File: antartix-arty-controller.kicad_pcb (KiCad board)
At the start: 4 copper layers, 96 x 40 mm, 163 parts, among them IC1 FT2232D, IC2 TPD8S009DSMR, J1 QTE-020-04-L-D-A, J10 3-794680-8, J11 1-794610-1, J12 1-794610-1, J13 1-794610-1, J14 1-794610-1, J15 3-794617-8, J16 1-794610-1, J17 1-794610-1, J18 1-794610-1, J19 1-794610-1, J2 0022232041, J3 614004185023, J4 WE_629105150521, J5 614004185023, J6 614004185023, J7 QTE-020-04-L-D-A, J8 WE_629105150521, J9 WE_685119136923, Q1 FDC6330L, Q2 FDC6330L, Q3 FDC6330L, U1 PCT2075GVX, U2 PAC1934T-I_JQ, U3 USB2514B-I_M2, U4 TPS2024DR, U5 TPS2024DR, U6 TPS2024DR, U7 FT230XS-R, Y1 7C-24.000MBB-T, Y2 MQ-6.000-12-30_30_

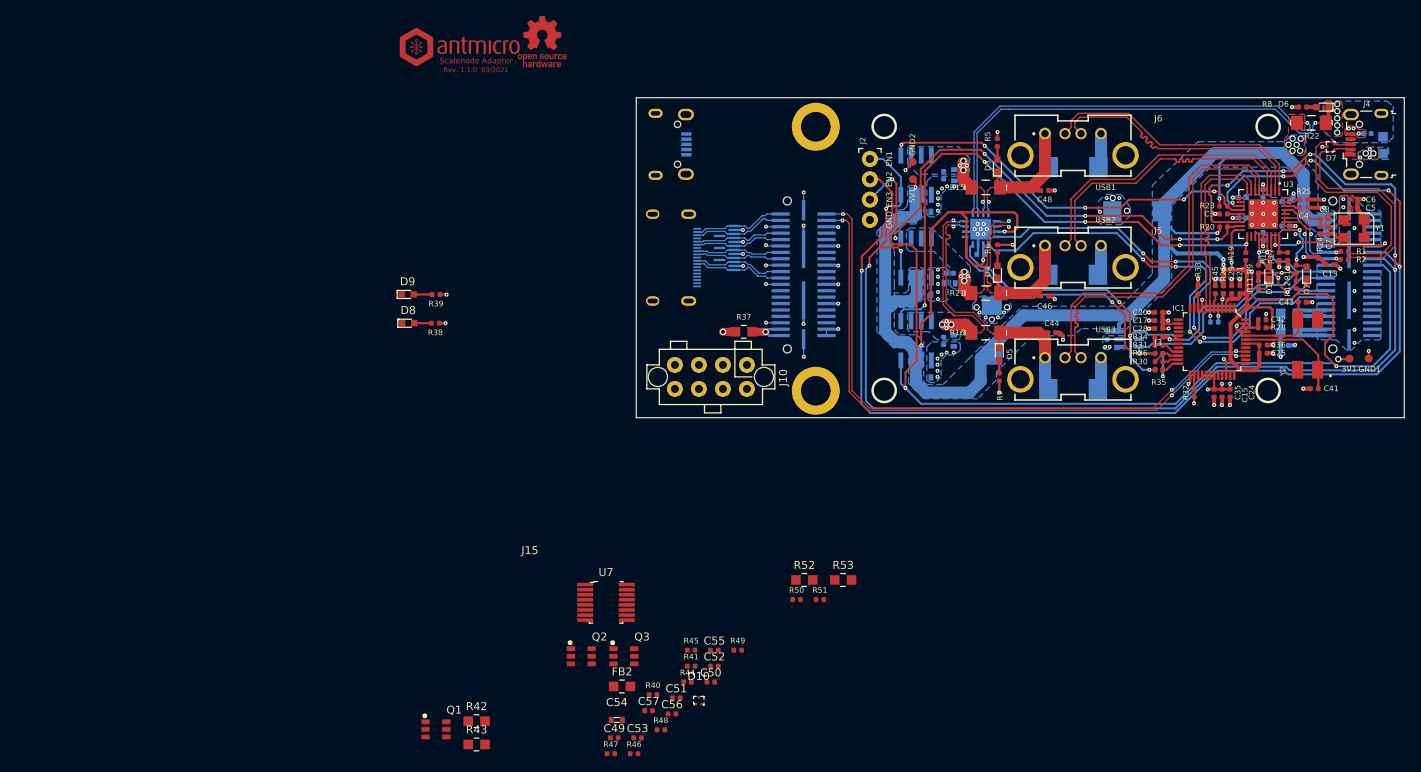
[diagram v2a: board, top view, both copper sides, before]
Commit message: Route buttons and HDMI
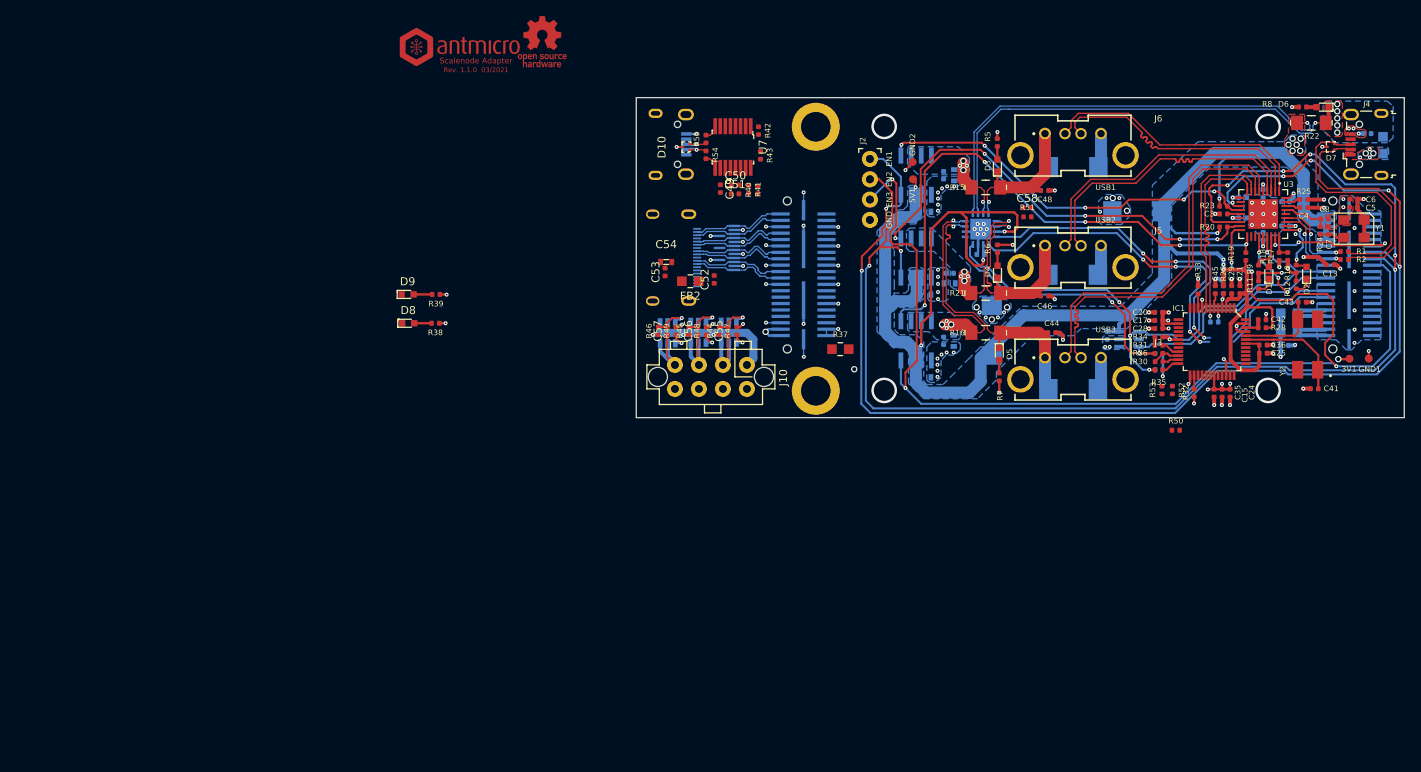
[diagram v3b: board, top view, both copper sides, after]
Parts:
- added C58: C_100n_0402, antartix-arty-controller-footprints:0402-cap, F.Cu at (190.9, 86.3)
- added R54: R_22R_0402, antartix-arty-controller-footprints:0402-res, F.Cu at (150.7, 79.7)
- added R55: R_22R_0402, antartix-arty-controller-footprints:0402-res, F.Cu at (150.7, 77.7)
- J11, J12, J13, J14, J15, J16, J17, J18, J19, Q1, Q2, Q3: moved to B.Cu
- R42, R43, R52, R53: value R_0R_0805 -> R_0R_0402; footprint antmicro-footprints:0805-res -> antartix-arty-controller-footprints:0402-res
- moved R42 81.8 mm to (157.3, 76.6), turned to 270 degrees
- moved R43 81.7 mm to (157.5, 79.7), turned to 270 degrees
- moved C49 69.9 mm to (152.5, 83.9), turned to 270 degrees
- moved D10 69.2 mm to (148.3, 78.7), turned to 90 degrees
- moved R40 64.5 mm to (157.2, 84.0), turned to 90 degrees
- moved C51 63.4 mm to (154.3, 84.5)
- moved C50 62.2 mm to (154.4, 83.4)
- moved Q1 61.7 mm to (153.6, 101.8), turned to 90 degrees
- moved R41 60.0 mm to (156.0, 84.0), turned to 270 degrees
- moved U7 59.1 mm to (154.1, 78.7), turned to 270 degrees
- moved C53 58.3 mm to (145.6, 94.3), turned to 90 degrees
- moved C54 57.6 mm to (145.7, 93.1)
- moved R47 55.2 mm to (154.6, 101.7), turned to 90 degrees
- moved R51 54.4 mm to (190.9, 87.4)
- moved R46 52.9 mm to (144.8, 101.7), turned to 90 degrees
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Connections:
- IC1 pad 39: RXD0 -> RXD1
- IC1 pad 40: TXD0 -> TXD1
- IC2 pad 13: VCC3V3 -> VCC5V0
- IC2 pad 15: VCC3V3 -> VCC5V0
- U7 pad 8: /antartix hdmi adapter/USB_CON_P -> Net-(R55-Pad2)
- U7 pad 9: /antartix hdmi adapter/USB_CON_N -> Net-(R54-Pad2)
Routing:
- net TXD0: track 78.0 -> 0.00 mm, vias 3 -> 0
- net RXD0: track 77.5 -> 0.00 mm, vias 3 -> 0
- net /antartix hdmi adapter/VCC_9V_IN: track 0.00 -> 22.7 mm, vias 0 -> 3
- net /antartix usb adapter/SLOW_~ALERT: track 59.6 -> 41.8 mm
- net /antartix usb adapter/~PWRDN: track 57.9 -> 40.1 mm
- net LED0: track 0.00 -> 15.1 mm
- net LED1: track 0.00 -> 14.8 mm
- net /antartix hdmi adapter/VCC_9V_OUT_3: track 0.00 -> 10.9 mm
- net /antartix hdmi adapter/VCC_9V_OUT_1: track 0.00 -> 10.2 mm
- net /antartix hdmi adapter/VCC_9V_OUT_2: track 0.00 -> 9.66 mm
- net GND: track 94.3 -> 99.1 mm, vias 117 -> 122
- net Net-(C55-Pad2): track 0.00 -> 4.65 mm, vias 0 -> 1
- net Net-(C56-Pad2): track 0.00 -> 4.60 mm, vias 0 -> 1
- net Net-(C57-Pad2): track 0.00 -> 4.53 mm, vias 0 -> 1
- net /antartix hdmi adapter/USB_CON_N: track 0.00 -> 3.44 mm, vias 0 -> 1
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
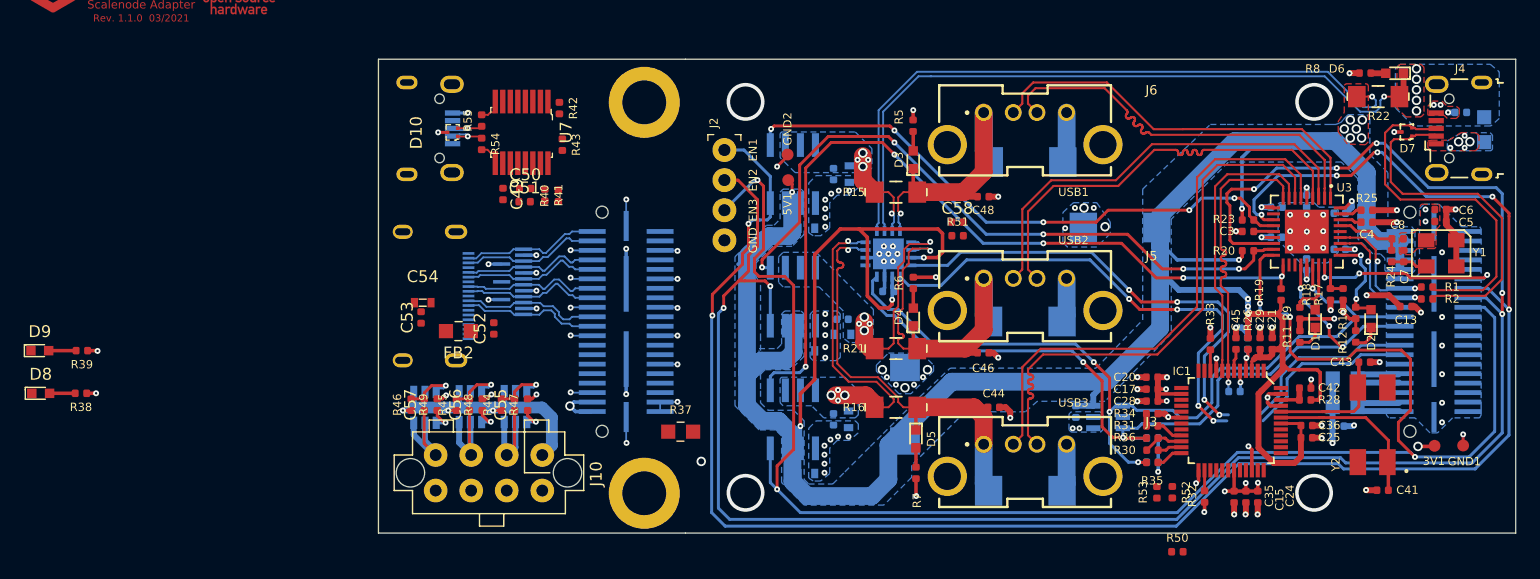
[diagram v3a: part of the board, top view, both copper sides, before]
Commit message: Route console and HDMI control signals
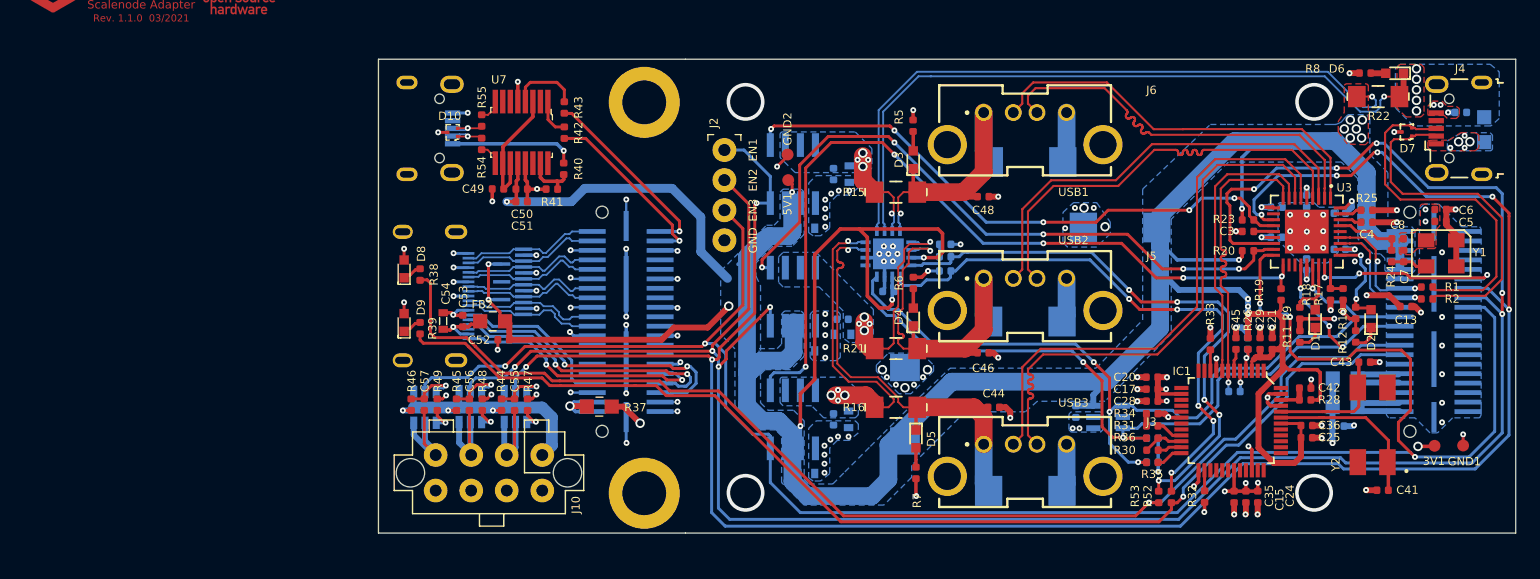
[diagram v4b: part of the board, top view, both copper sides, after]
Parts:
- C58, R50, R51: moved to B.Cu
- moved D8 32.4 mm to (144.2, 90.2), turned to 90 degrees
- moved D9 30.8 mm to (144.2, 94.7), turned to 90 degrees
- moved R50 30.8 mm to (189.8, 90.4)
- moved R38 30.3 mm to (145.5, 90.7), turned to 270 degrees
- moved R39 28.6 mm to (145.5, 95.2), turned to 270 degrees
- moved R37 7.19 mm to (160.6, 101.8), turned to 180 degrees
- moved C53 3.53 mm to (149.1, 94.6)
- moved R43 3.14 mm to (157.7, 76.6)
- moved FB2 3.01 mm to (151.6, 94.6)
- moved C54 2.32 mm to (147.5, 94.6), turned to 270 degrees
- moved R40 2.32 mm to (157.6, 81.8), turned to 270 degrees
- moved C58 2.14 mm to (189.8, 88.1)
- moved R42 2.12 mm to (157.7, 78.7)
- moved R51 2.06 mm to (189.8, 89.2)
- moved C52 1.26 mm to (152.6, 96.2), turned to 180 degrees
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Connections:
- D8 pad 1: LED0 -> Net-(D8-Pad1)
- D8 pad 2: Net-(D8-Pad2) -> GND
- D9 pad 1: LED1 -> Net-(D9-Pad1)
- D9 pad 2: Net-(D9-Pad2) -> GND
- R38 pad 1: GND -> Net-(D8-Pad1)
- R38 pad 2: Net-(D8-Pad2) -> LED0
- R39 pad 1: GND -> Net-(D9-Pad1)
- R39 pad 2: Net-(D9-Pad2) -> LED1
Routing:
- net LED0: track 15.1 -> 101.1 mm, vias 0 -> 1
- net LED1: track 14.8 -> 97.1 mm, vias 0 -> 1
- net VCC5V0: track 302.8 -> 359.0 mm, vias 18 -> 20
- net HDMI0_SCL: track 0.00 -> 25.7 mm, vias 0 -> 2
- net GND: track 99.1 -> 124.6 mm, vias 122 -> 135
- net HDMI0_SDA: track 0.00 -> 24.0 mm, vias 0 -> 2
- net USB2_EN: track 165.3 -> 189.0 mm, vias 7 -> 9
- net HDMI0_HOTPLUG: track 0.00 -> 21.8 mm, vias 0 -> 2
- net USB1_EN: track 158.6 -> 177.4 mm, vias 7 -> 8
- net USB3_EN: track 145.2 -> 163.3 mm
- net TXD0: track 0.00 -> 16.0 mm, vias 0 -> 1
- net RXD0: track 0.00 -> 15.4 mm, vias 0 -> 1
- net HDMI0_CEC: track 0.00 -> 13.8 mm
- net Net-(C49-Pad1): track 0.00 -> 10.7 mm
- net Net-(J8-Pad1): track 0.00 -> 10.7 mm, vias 0 -> 1
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
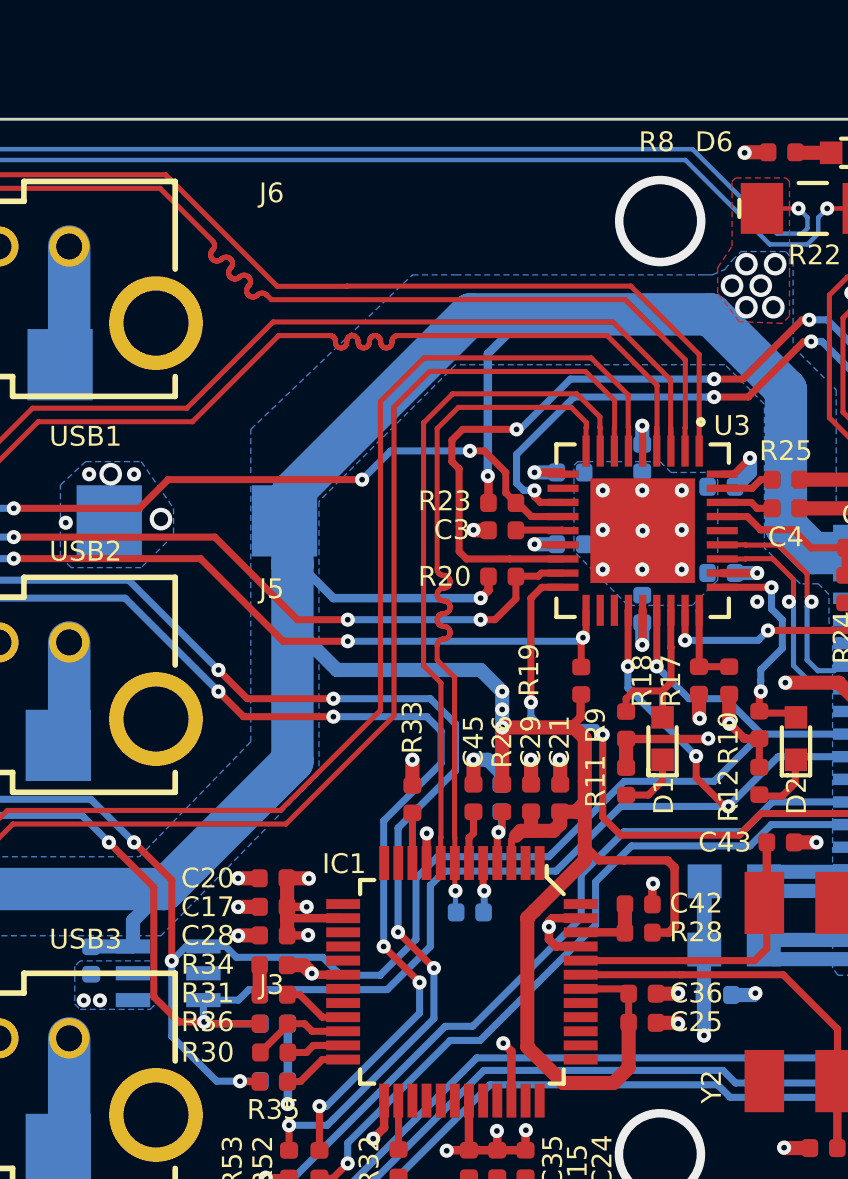
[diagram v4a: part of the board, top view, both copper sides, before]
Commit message: Add 22R to FTDI
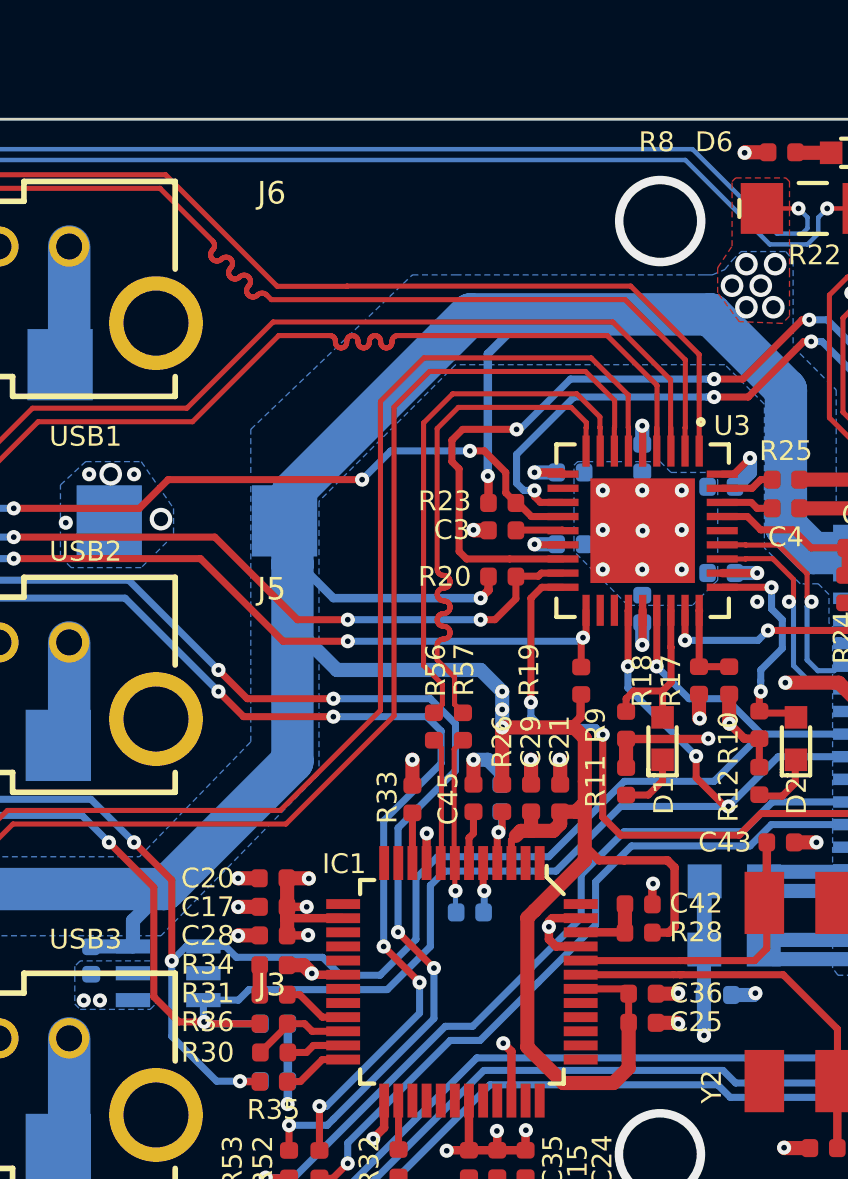
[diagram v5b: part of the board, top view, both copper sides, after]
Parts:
- added R56: R_22R_0402, antartix-arty-controller-footprints:0402-res, F.Cu at (213.0, 94.0)
- added R57: R_22R_0402, antartix-arty-controller-footprints:0402-res, F.Cu at (214.0, 94.0)
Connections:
- IC1 pad 7: /antartix usb adapter/USB_D_FTDI_P -> Net-(IC1-Pad7)
- IC1 pad 8: /antartix usb adapter/USB_D_FTDI_N -> Net-(IC1-Pad8)
- R29 pad 1: /antartix usb adapter/USB_D_FTDI_P -> Net-(IC1-Pad7)
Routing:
- net /antartix usb adapter/USB_D_FTDI_P: track 25.8 -> 18.8 mm, vias 1 -> 0
- net Net-(IC1-Pad7): track 0.00 -> 6.23 mm, vias 0 -> 1
- net /antartix usb adapter/USB_D_FTDI_N: track 24.0 -> 18.9 mm
- net Net-(IC1-Pad8): track 0.00 -> 4.46 mm
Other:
- net class HDMI added: clearance 0.127, trace_width 0.25, via_dia 0.5, via_drill 0.2

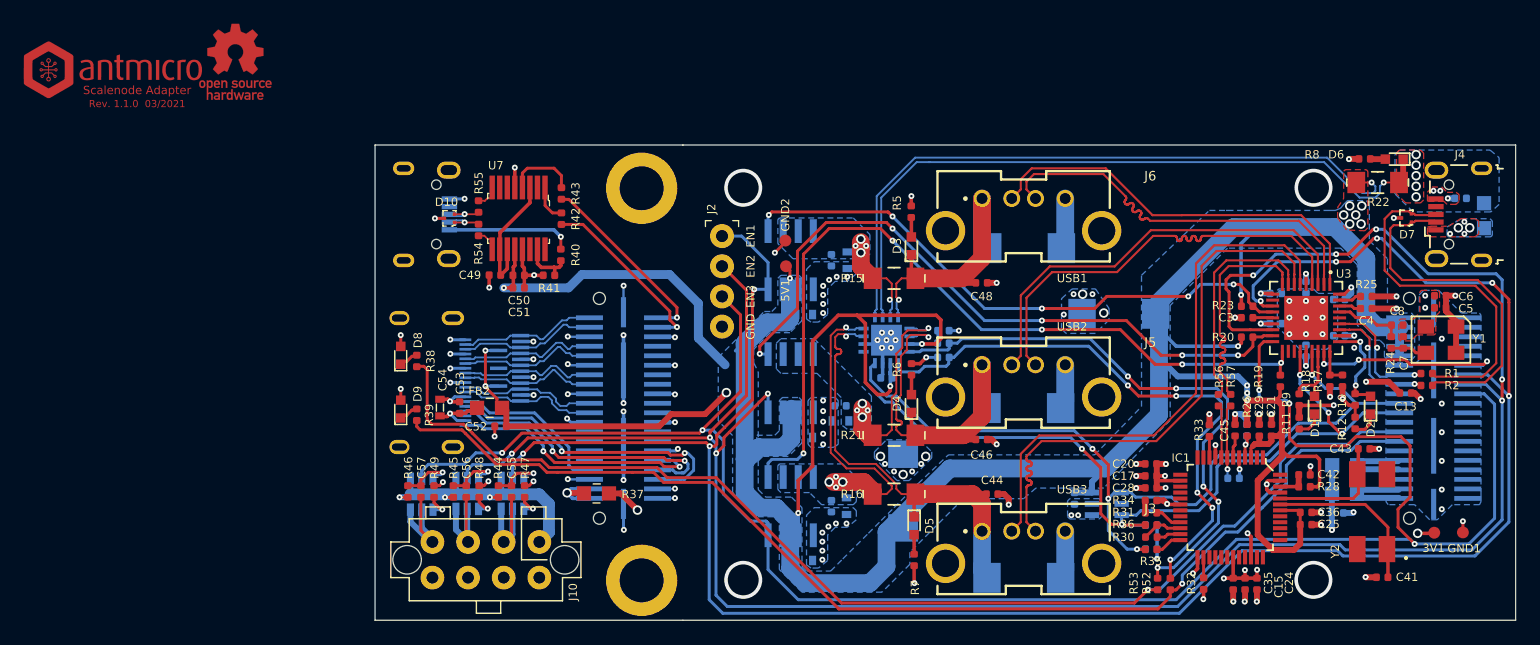
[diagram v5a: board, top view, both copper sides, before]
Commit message: Place logotypes on PCB
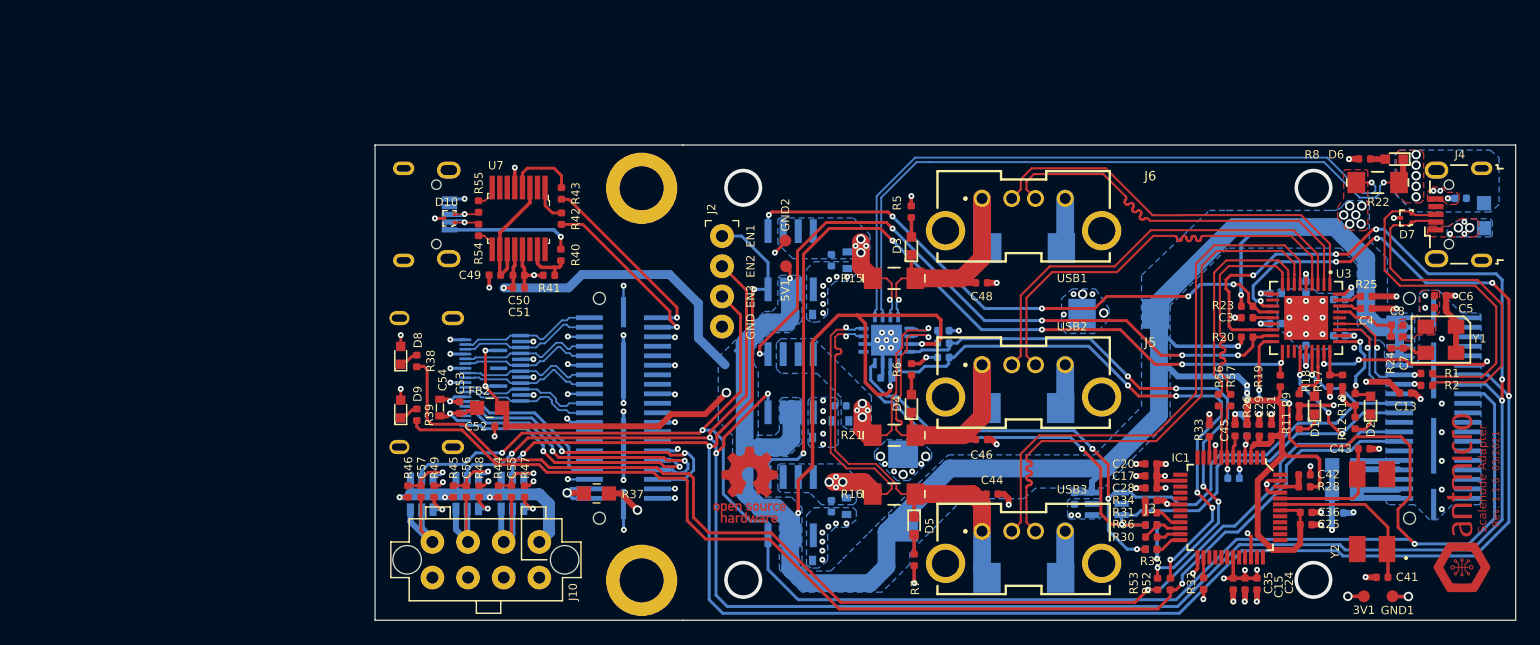
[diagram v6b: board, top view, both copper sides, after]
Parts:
- moved N1 118.7 mm to (233.5, 102.2), turned to 90 degrees
- moved N2 56.0 mm to (173.5, 101.1)
- moved GND1 8.00 mm to (227.6, 110.4)
- moved 3V1 7.98 mm to (225.2, 110.5)
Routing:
- net LED1: track 97.1 -> 99.0 mm
- net LED0: track 101.1 -> 103.0 mm
